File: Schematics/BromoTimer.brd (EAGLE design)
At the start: 49.2 x 71.1 mm, 20 parts, among them IC1 PIC16F687, IC2 7805TV, K1 351, K2 351, Q1 2N3565, Q2 2N3565, X4 22-23-2021

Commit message: Fixed bug in schematics
The poles on the diode bridge were inverted.
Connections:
- net GND: now also B1.-; no longer B1.+
- net V+: now also B1.+; no longer B1.-
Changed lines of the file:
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@@
 <?xml version="1.0" encoding="utf-8"?>
 <!DOCTYPE eagle SYSTEM "eagle.dtd">
-<eagle version="6.2">
+<eagle version="6.3">
 <drawing>
 <settings>
@@
 <contactref element="Q2" pad="3"/>
 <contactref element="C1" pad="-"/>
-<contactref element="B1" pad="+"/>
 <contactref element="SV1" pad="1"/>
 <contactref element="X4" pad="1"/>
-<wire x1="19.05" y1="67.31" x2="46.99" y2="67.31" width="0" layer="19" extent="1-1"/>
-<wire x1="2.54" y1="67.31" x2="19.05" y2="67.31" width="0" layer="19" extent="1-1"/>
-<wire x1="12.7" y1="52.07" x2="19.05" y2="67.31" width="0" layer="19" extent="1-1"/>
-<wire x1="8.382" y1="41.91" x2="12.7" y2="52.07" width="0" layer="19" extent="1-1"/>
-<wire x1="2.54" y1="41.91" x2="8.382" y2="41.91" width="0" layer="19" extent="1-1"/>
-<wire x1="5.08" y1="29.21" x2="2.54" y2="41.91" width="0" layer="19" extent="1-1"/>
-<wire x1="42.545" y1="50.8" x2="2.54" y2="41.91" width="0" layer="19" extent="1-1"/>
+<contactref element="B1" pad="-"/>
+<wire x1="42.545" y1="50.8" x2="46.99" y2="67.31" width="0" layer="19" extent="1-1"/>
 <wire x1="44.45" y1="36.83" x2="42.545" y2="50.8" width="0" layer="19" extent="1-1"/>
 <wire x1="29.21" y1="36.83" x2="44.45" y2="36.83" width="0" layer="19" extent="1-1"/>
-<wire x1="5.08" y1="50.8" x2="29.21" y2="36.83" width="0" layer="19" extent="1-1"/>
+<wire x1="10.16" y1="34.29" x2="29.21" y2="36.83" width="0" layer="19" extent="1-1"/>
+<wire x1="8.382" y1="41.91" x2="10.16" y2="34.29" width="0" layer="19" extent="1-1"/>
+<wire x1="2.54" y1="41.91" x2="8.382" y2="41.91" width="0" layer="19" extent="1-1"/>
+<wire x1="5.08" y1="50.8" x2="2.54" y2="41.91" width="0" layer="19" extent="1-1"/>
+<wire x1="12.7" y1="52.07" x2="5.08" y2="50.8" width="0" layer="19" extent="1-1"/>
 <wire x1="3.81" y1="58.42" x2="5.08" y2="50.8" width="0" layer="19" extent="1-1"/>
+<wire x1="2.54" y1="67.31" x2="3.81" y2="58.42" width="0" layer="19" extent="1-1"/>
+<wire x1="19.05" y1="67.31" x2="12.7" y2="52.07" width="0" layer="19" extent="1-1"/>
 </signal>
 <signal name="RS">
@@
 </signal>
 <signal name="V+">
-<contactref element="B1" pad="-"/>
 <contactref element="C1" pad="+"/>
 <contactref element="IC2" pad="1"/>
-<wire x1="10.16" y1="34.29" x2="11.938" y2="41.91" width="0" layer="19" extent="1-1"/>
-<wire x1="2.54" y1="39.37" x2="10.16" y2="34.29" width="0" layer="19" extent="1-1"/>
+<contactref element="B1" pad="+"/>
+<wire x1="2.54" y1="39.37" x2="11.938" y2="41.91" width="0" layer="19" extent="1-1"/>
+<wire x1="5.08" y1="29.21" x2="2.54" y2="39.37" width="0" layer="19" extent="1-1"/>
 </signal>
 <signal name="N$13">

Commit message: Use 12V relay.
Use 12V relay since V relays are not common.
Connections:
- net +5V: no longer K1.1, K2.1
- net V+: now also K1.1, K2.1
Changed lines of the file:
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@@
 <contactref element="SV2" pad="2"/>
 <contactref element="R1" pad="A"/>
-<contactref element="K1" pad="1"/>
-<contactref element="K2" pad="1"/>
+<wire x1="21.59" y1="67.31" x2="42.545" y2="57.15" width="0" layer="19" extent="1-1"/>
 <wire x1="12.7" y1="59.69" x2="21.59" y2="67.31" width="0" layer="19" extent="1-1"/>
-<wire x1="26.67" y1="31.75" x2="12.7" y2="59.69" width="0" layer="19" extent="1-1"/>
-<wire x1="39.37" y1="31.75" x2="26.67" y2="31.75" width="0" layer="19" extent="1-1"/>
-<wire x1="2.54" y1="44.45" x2="39.37" y2="31.75" width="0" layer="19" extent="1-1"/>
-<wire x1="2.54" y1="50.8" x2="2.54" y2="44.45" width="0" layer="19" extent="1-1"/>
-<wire x1="42.545" y1="57.15" x2="2.54" y2="50.8" width="0" layer="19" extent="1-1"/>
+<wire x1="2.54" y1="50.8" x2="12.7" y2="59.69" width="0" layer="19" extent="1-1"/>
+<wire x1="2.54" y1="44.45" x2="2.54" y2="50.8" width="0" layer="19" extent="1-1"/>
 </signal>
 <signal name="GND">
@@
 <contactref element="IC2" pad="1"/>
 <contactref element="B1" pad="+"/>
+<contactref element="K2" pad="1"/>
+<contactref element="K1" pad="1"/>
+<wire x1="26.67" y1="31.75" x2="39.37" y2="31.75" width="0" layer="19" extent="1-1"/>
+<wire x1="11.938" y1="41.91" x2="26.67" y2="31.75" width="0" layer="19" extent="1-1"/>
 <wire x1="2.54" y1="39.37" x2="11.938" y2="41.91" width="0" layer="19" extent="1-1"/>
 <wire x1="5.08" y1="29.21" x2="2.54" y2="39.37" width="0" layer="19" extent="1-1"/>

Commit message: Add ICSP header
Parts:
- added D1, D2: 1N4148DO35-7, diode:DO35-7
- added SV3: (no value), con-lstb:MA05-1
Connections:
- new net N$15: IC1.4, SV3.1
- net +5V: now also SV3.2
- net A: now also SV3.4
- net B: now also SV3.5
- net GND: now also D1.A, D2.A, SV3.3
- net V+: now also D1.C, D2.C
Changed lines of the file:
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@@
 <attribute name="OC_FARNELL" value="1462926" x="44.45" y="102.87" size="1.778" layer="27" rot="R90" display="off"/>
+</element>
+<element name="D1" library="diode" package="DO35-7" value="1N4148DO35-7" x="3.81" y="-6.35"/>
+<element name="D2" library="diode" package="DO35-7" value="1N4148DO35-7" x="3.81" y="-12.7"/>
+<element name="SV3" library="con-lstb" package="MA05-1" value="" x="5.08" y="-20.32">
+<attribute name="OC_NEWARK" value="unknown" x="5.08" y="-20.32" size="1.778" layer="27" display="off"/>
+<attribute name="MPN" value="" x="5.08" y="-20.32" size="1.778" layer="27" display="off"/>
+<attribute name="MF" value="" x="5.08" y="-20.32" size="1.778" layer="27" display="off"/>
+<attribute name="OC_FARNELL" value="unknown" x="5.08" y="-20.32" size="1.778" layer="27" display="off"/>
 </element>
 </elements>
@@
 <contactref element="SV2" pad="2"/>
 <contactref element="R1" pad="A"/>
+<contactref element="SV3" pad="2"/>
 <wire x1="21.59" y1="67.31" x2="42.545" y2="57.15" width="0" layer="19" extent="1-1"/>
 <wire x1="12.7" y1="59.69" x2="21.59" y2="67.31" width="0" layer="19" extent="1-1"/>
 <wire x1="2.54" y1="50.8" x2="12.7" y2="59.69" width="0" layer="19" extent="1-1"/>
 <wire x1="2.54" y1="44.45" x2="2.54" y2="50.8" width="0" layer="19" extent="1-1"/>
+<wire x1="2.54" y1="-20.32" x2="2.54" y2="44.45" width="0" layer="19" extent="1-1"/>
 </signal>
 <signal name="GND">
@@
 <contactref element="X4" pad="1"/>
 <contactref element="B1" pad="-"/>
+<contactref element="D2" pad="A"/>
+<contactref element="D1" pad="A"/>
+<contactref element="SV3" pad="3"/>
 <wire x1="42.545" y1="50.8" x2="46.99" y2="67.31" width="0" layer="19" extent="1-1"/>
 <wire x1="44.45" y1="36.83" x2="42.545" y2="50.8" width="0" layer="19" extent="1-1"/>
@@
 <wire x1="2.54" y1="67.31" x2="3.81" y2="58.42" width="0" layer="19" extent="1-1"/>
 <wire x1="19.05" y1="67.31" x2="12.7" y2="52.07" width="0" layer="19" extent="1-1"/>
+<wire x1="7.62" y1="-6.35" x2="10.16" y2="34.29" width="0" layer="19" extent="1-1"/>
+<wire x1="7.62" y1="-12.7" x2="7.62" y2="-6.35" width="0" layer="19" extent="1-1"/>
+<wire x1="5.08" y1="-20.32" x2="7.62" y2="-12.7" width="0" layer="19" extent="1-1"/>
 </signal>
 <signal name="RS">
@@
 <contactref element="SV1" pad="5"/>
 <contactref element="IC1" pad="19"/>
+<contactref element="SV3" pad="4"/>
 <wire x1="15.24" y1="59.69" x2="12.7" y2="67.31" width="0" layer="19" extent="1-1"/>
+<wire x1="7.62" y1="-20.32" x2="15.24" y2="59.69" width="0" layer="19" extent="1-1"/>
 </signal>
 <signal name="B">
 <contactref element="SV1" pad="6"/>
 <contactref element="IC1" pad="18"/>
+<contactref element="SV3" pad="5"/>
 <wire x1="17.78" y1="59.69" x2="15.24" y2="67.31" width="0" layer="19" extent="1-1"/>
+<wire x1="10.16" y1="-20.32" x2="17.78" y2="59.69" width="0" layer="19" extent="1-1"/>
 </signal>
 <signal name="N$4">
@@
 <contactref element="K2" pad="1"/>
 <contactref element="K1" pad="1"/>
+<contactref element="D2" pad="C"/>
+<contactref element="D1" pad="C"/>
 <wire x1="26.67" y1="31.75" x2="39.37" y2="31.75" width="0" layer="19" extent="1-1"/>
 <wire x1="11.938" y1="41.91" x2="26.67" y2="31.75" width="0" layer="19" extent="1-1"/>
 <wire x1="2.54" y1="39.37" x2="11.938" y2="41.91" width="0" layer="19" extent="1-1"/>
 <wire x1="5.08" y1="29.21" x2="2.54" y2="39.37" width="0" layer="19" extent="1-1"/>
+<wire x1="0" y1="-6.35" x2="5.08" y2="29.21" width="0" layer="19" extent="1-1"/>
+<wire x1="0" y1="-12.7" x2="0" y2="-6.35" width="0" layer="19" extent="1-1"/>
 </signal>
 <signal name="N$13">
@@
 <wire x1="20.32" y1="41.91" x2="25.4" y2="52.07" width="0" layer="19" extent="1-1"/>
 </signal>
+<signal name="N$15">
+<contactref element="SV3" pad="1"/>
+<contactref element="IC1" pad="4"/>
+<wire x1="0" y1="-20.32" x2="20.32" y2="52.07" width="0" layer="19" extent="1-1"/>
+</signal>
 </signals>

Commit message: Add buzzer and diode protection to 7805.
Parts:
- added D3: 1N4148DO35-7, diode:DO35-7
- added Q3: 2N3565, transistor-npn:TO92
- added R5: (no value), rcl:0207/10
- added X5: 22-23-2021, con-molex:22-23-2021
- SV1: value (none) -> ENCODER
- SV2: value (none) -> DISPLAY
- SV3: value (none) -> ICSP
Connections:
- new net N$17: IC1.5, R5.2
- new net N$18: Q3.2, R5.1
- new net N$19: Q3.3, X5.1
- net +5V: now also D3.A
- net GND: now also Q3.1
- net SW: now also IC1.2
- net V+: now also D3.C, X5.2
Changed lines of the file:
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@@
 <elements>
 <element name="IC1" library="ic-package" package="SOCKET-20" value="PIC16F687" x="24.13" y="55.88"/>
-<element name="SV1" library="con-lsta" package="FE06" value="" x="8.89" y="67.31">
+<element name="SV1" library="con-lsta" package="FE06" value="ENCODER" x="8.89" y="67.31">
 <attribute name="OC_NEWARK" value="unknown" x="62.23" y="7.62" size="1.778" layer="27" display="off"/>
 <attribute name="MPN" value="" x="62.23" y="7.62" size="1.778" layer="27" display="off"/>
@@
 <attribute name="OC_FARNELL" value="unknown" x="62.23" y="7.62" size="1.778" layer="27" display="off"/>
 </element>
-<element name="SV2" library="con-lsta" package="FE12" value="" x="33.02" y="67.31">
+<element name="SV2" library="con-lsta" package="FE12" value="DISPLAY" x="33.02" y="67.31">
 <attribute name="OC_NEWARK" value="unknown" x="62.23" y="7.62" size="1.778" layer="27" display="off"/>
 <attribute name="MPN" value="" x="62.23" y="7.62" size="1.778" layer="27" display="off"/>
@@
 <element name="D1" library="diode" package="DO35-7" value="1N4148DO35-7" x="3.81" y="-6.35"/>
 <element name="D2" library="diode" package="DO35-7" value="1N4148DO35-7" x="3.81" y="-12.7"/>
-<element name="SV3" library="con-lstb" package="MA05-1" value="" x="5.08" y="-20.32">
+<element name="SV3" library="con-lstb" package="MA05-1" value="ICSP" x="5.08" y="-20.32">
 <attribute name="OC_NEWARK" value="unknown" x="5.08" y="-20.32" size="1.778" layer="27" display="off"/>
 <attribute name="MPN" value="" x="5.08" y="-20.32" size="1.778" layer="27" display="off"/>
@@
 <attribute name="OC_FARNELL" value="unknown" x="5.08" y="-20.32" size="1.778" layer="27" display="off"/>
 </element>
+<element name="D3" library="diode" package="DO35-7" value="1N4148DO35-7" x="3.81" y="-27.94"/>
+<element name="Q3" library="transistor-npn" package="TO92" value="2N3565" x="0" y="-34.29"/>
+<element name="R5" library="rcl" package="0207/10" value="" x="3.81" y="-39.37"/>
+<element name="X5" library="con-molex" package="22-23-2021" value="22-23-2021" x="-6.35" y="-34.29">
+<attribute name="OC_NEWARK" value="25C3832" x="-6.35" y="-34.29" size="1.778" layer="27" display="off"/>
+<attribute name="MPN" value="22-23-2021" x="-6.35" y="-34.29" size="1.778" layer="27" display="off"/>
+<attribute name="MF" value="MOLEX" x="-6.35" y="-34.29" size="1.778" layer="27" display="off"/>
+<attribute name="OC_FARNELL" value="1462926" x="-6.35" y="-34.29" size="1.778" layer="27" display="off"/>
+</element>
 </elements>
 <signals>
 <signal name="+5V">
-<contactref element="IC2" pad="3"/>
-<contactref element="C2" pad="+"/>
 <contactref element="IC1" pad="20"/>
 <contactref element="SV2" pad="2"/>
 <contactref element="R1" pad="A"/>
 <contactref element="SV3" pad="2"/>
+<contactref element="IC2" pad="3"/>
+<contactref element="C2" pad="+"/>
+<contactref element="D3" pad="A"/>
 <wire x1="21.59" y1="67.31" x2="42.545" y2="57.15" width="0" layer="19" extent="1-1"/>
 <wire x1="12.7" y1="59.69" x2="21.59" y2="67.31" width="0" layer="19" extent="1-1"/>
@@
 <wire x1="2.54" y1="44.45" x2="2.54" y2="50.8" width="0" layer="19" extent="1-1"/>
 <wire x1="2.54" y1="-20.32" x2="2.54" y2="44.45" width="0" layer="19" extent="1-1"/>
+<wire x1="7.62" y1="-27.94" x2="2.54" y2="-20.32" width="0" layer="19" extent="1-1"/>
 </signal>
 <signal name="GND">
@@
 <contactref element="D1" pad="A"/>
 <contactref element="SV3" pad="3"/>
+<contactref element="Q3" pad="1"/>
 <wire x1="42.545" y1="50.8" x2="46.99" y2="67.31" width="0" layer="19" extent="1-1"/>
 <wire x1="44.45" y1="36.83" x2="42.545" y2="50.8" width="0" layer="19" extent="1-1"/>
@@
 <wire x1="7.62" y1="-12.7" x2="7.62" y2="-6.35" width="0" layer="19" extent="1-1"/>
 <wire x1="5.08" y1="-20.32" x2="7.62" y2="-12.7" width="0" layer="19" extent="1-1"/>
+<wire x1="1.27" y1="-34.29" x2="5.08" y2="-20.32" width="0" layer="19" extent="1-1"/>
 </signal>
 <signal name="RS">
@@
 <signal name="SW">
 <contactref element="SV1" pad="4"/>
+<contactref element="IC1" pad="2"/>
+<wire x1="15.24" y1="52.07" x2="10.16" y2="67.31" width="0" layer="19" extent="1-1"/>
 </signal>
 <signal name="A">
@@
 <contactref element="D2" pad="C"/>
 <contactref element="D1" pad="C"/>
+<contactref element="D3" pad="C"/>
+<contactref element="X5" pad="2"/>
 <wire x1="26.67" y1="31.75" x2="39.37" y2="31.75" width="0" layer="19" extent="1-1"/>
 <wire x1="11.938" y1="41.91" x2="26.67" y2="31.75" width="0" layer="19" extent="1-1"/>
@@
 <wire x1="0" y1="-6.35" x2="5.08" y2="29.21" width="0" layer="19" extent="1-1"/>
 <wire x1="0" y1="-12.7" x2="0" y2="-6.35" width="0" layer="19" extent="1-1"/>
+<wire x1="0" y1="-27.94" x2="0" y2="-12.7" width="0" layer="19" extent="1-1"/>
+<wire x1="-5.08" y1="-34.29" x2="0" y2="-27.94" width="0" layer="19" extent="1-1"/>
 </signal>
 <signal name="N$13">
@@
 <wire x1="0" y1="-20.32" x2="20.32" y2="52.07" width="0" layer="19" extent="1-1"/>
 </signal>
+<signal name="N$17">
+<contactref element="R5" pad="2"/>
+<contactref element="IC1" pad="5"/>
+<wire x1="8.89" y1="-39.37" x2="22.86" y2="52.07" width="0" layer="19" extent="1-1"/>
+</signal>
+<signal name="N$18">
+<contactref element="R5" pad="1"/>
+<contactref element="Q3" pad="2"/>
+<wire x1="0" y1="-32.385" x2="-1.27" y2="-39.37" width="0" layer="19" extent="1-1"/>
+</signal>
+<signal name="N$19">
+<contactref element="Q3" pad="3"/>
+<contactref element="X5" pad="1"/>
+<wire x1="-1.27" y1="-34.29" x2="-7.62" y2="-34.29" width="0" layer="19" extent="1-1"/>
+</signal>
 </signals>

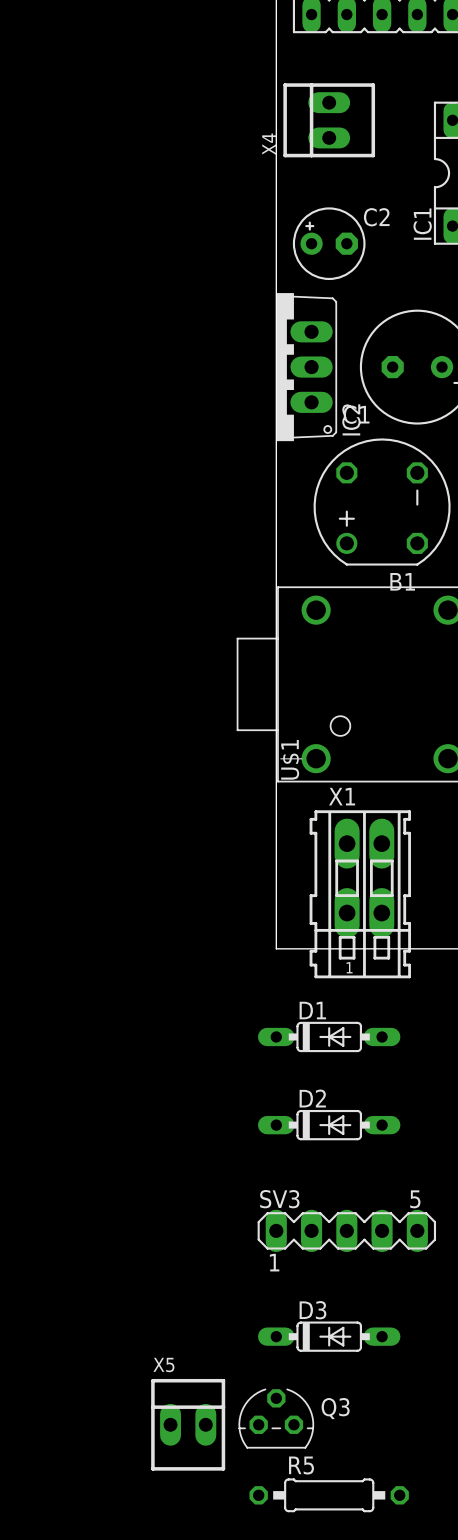
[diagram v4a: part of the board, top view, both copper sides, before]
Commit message: Add support for external LED
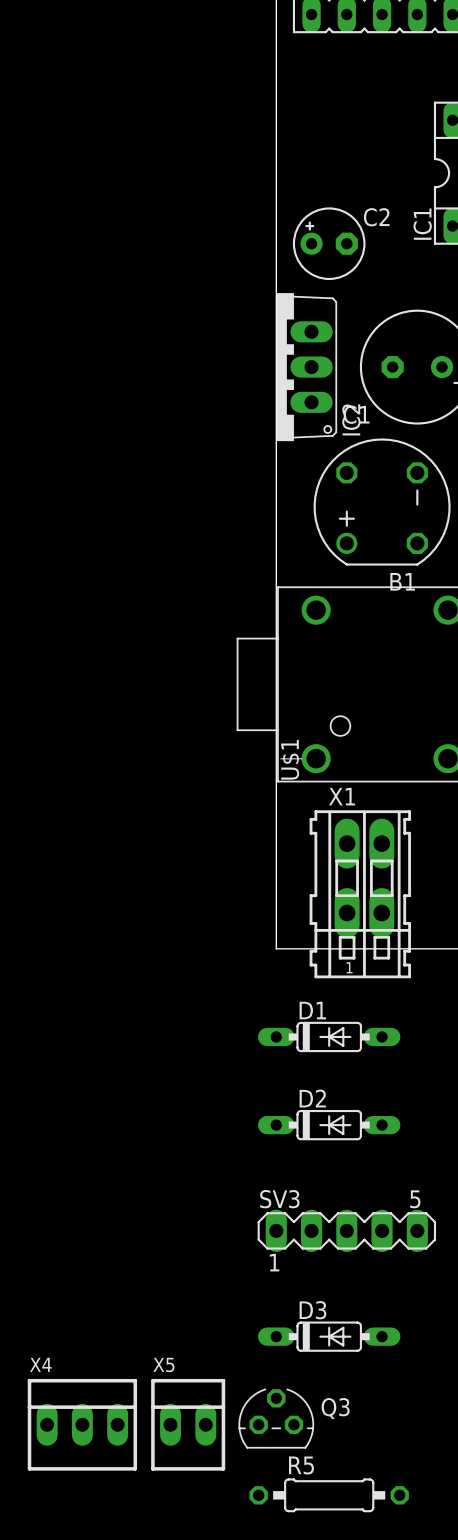
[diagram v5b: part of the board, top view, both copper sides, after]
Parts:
- X4: value 22-23-2021 -> 22-23-2031; device con-molex:22-23-2021 -> con-molex:22-23-2031
- X5: value 22-23-2021 -> BUZZER
- moved X4 95.6 mm to (-14.0, -34.3), turned to 0 degrees
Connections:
- new net N$20: IC1.3, X4.1
- net GND: now also X4.3; no longer X4.1
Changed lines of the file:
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@@
 <element name="U$1" library="SparkFun" package="TRANSFORMER" value="TRANSFORMERPTH" x="7.62" y="19.05" rot="R90"/>
 <element name="B1" library="rectifier" package="RB1A" value="" x="7.62" y="31.75" rot="R90"/>
-<element name="X4" library="con-molex" package="22-23-2021" value="22-23-2021" x="3.81" y="59.69" rot="R90">
-<attribute name="OC_NEWARK" value="25C3832" x="44.45" y="102.87" size="1.778" layer="27" rot="R90" display="off"/>
-<attribute name="MPN" value="22-23-2021" x="44.45" y="102.87" size="1.778" layer="27" rot="R90" display="off"/>
-<attribute name="MF" value="MOLEX" x="44.45" y="102.87" size="1.778" layer="27" rot="R90" display="off"/>
-<attribute name="OC_FARNELL" value="1462926" x="44.45" y="102.87" size="1.778" layer="27" rot="R90" display="off"/>
-</element>
 <element name="D1" library="diode" package="DO35-7" value="1N4148DO35-7" x="3.81" y="-6.35"/>
 <element name="D2" library="diode" package="DO35-7" value="1N4148DO35-7" x="3.81" y="-12.7"/>
@@
 <element name="Q3" library="transistor-npn" package="TO92" value="2N3565" x="0" y="-34.29"/>
 <element name="R5" library="rcl" package="0207/10" value="" x="3.81" y="-39.37"/>
-<element name="X5" library="con-molex" package="22-23-2021" value="22-23-2021" x="-6.35" y="-34.29">
+<element name="X5" library="con-molex" package="22-23-2021" value="BUZZER" x="-6.35" y="-34.29">
 <attribute name="OC_NEWARK" value="25C3832" x="-6.35" y="-34.29" size="1.778" layer="27" display="off"/>
 <attribute name="MPN" value="22-23-2021" x="-6.35" y="-34.29" size="1.778" layer="27" display="off"/>
 <attribute name="MF" value="MOLEX" x="-6.35" y="-34.29" size="1.778" layer="27" display="off"/>
 <attribute name="OC_FARNELL" value="1462926" x="-6.35" y="-34.29" size="1.778" layer="27" display="off"/>
+</element>
+<element name="X4" library="con-molex" package="22-23-2031" value="22-23-2031" x="-13.97" y="-34.29">
+<attribute name="OC_NEWARK" value="30C0862" x="-13.97" y="-34.29" size="1.778" layer="27" display="off"/>
+<attribute name="MPN" value="22-23-2031" x="-13.97" y="-34.29" size="1.778" layer="27" display="off"/>
+<attribute name="MF" value="MOLEX" x="-13.97" y="-34.29" size="1.778" layer="27" display="off"/>
+<attribute name="OC_FARNELL" value="1462950" x="-13.97" y="-34.29" size="1.778" layer="27" display="off"/>
 </element>
 </elements>
@@
 <contactref element="C1" pad="-"/>
 <contactref element="SV1" pad="1"/>
-<contactref element="X4" pad="1"/>
 <contactref element="B1" pad="-"/>
 <contactref element="D2" pad="A"/>
@@
 <contactref element="SV3" pad="3"/>
 <contactref element="Q3" pad="1"/>
+<contactref element="X4" pad="3"/>
 <wire x1="42.545" y1="50.8" x2="46.99" y2="67.31" width="0" layer="19" extent="1-1"/>
 <wire x1="44.45" y1="36.83" x2="42.545" y2="50.8" width="0" layer="19" extent="1-1"/>
@@
 <wire x1="5.08" y1="50.8" x2="2.54" y2="41.91" width="0" layer="19" extent="1-1"/>
 <wire x1="12.7" y1="52.07" x2="5.08" y2="50.8" width="0" layer="19" extent="1-1"/>
-<wire x1="3.81" y1="58.42" x2="5.08" y2="50.8" width="0" layer="19" extent="1-1"/>
-<wire x1="2.54" y1="67.31" x2="3.81" y2="58.42" width="0" layer="19" extent="1-1"/>
 <wire x1="19.05" y1="67.31" x2="12.7" y2="52.07" width="0" layer="19" extent="1-1"/>
+<wire x1="2.54" y1="67.31" x2="19.05" y2="67.31" width="0" layer="19" extent="1-1"/>
 <wire x1="7.62" y1="-6.35" x2="10.16" y2="34.29" width="0" layer="19" extent="1-1"/>
 <wire x1="7.62" y1="-12.7" x2="7.62" y2="-6.35" width="0" layer="19" extent="1-1"/>
 <wire x1="5.08" y1="-20.32" x2="7.62" y2="-12.7" width="0" layer="19" extent="1-1"/>
 <wire x1="1.27" y1="-34.29" x2="5.08" y2="-20.32" width="0" layer="19" extent="1-1"/>
+<wire x1="-11.43" y1="-34.29" x2="1.27" y2="-34.29" width="0" layer="19" extent="1-1"/>
 </signal>
 <signal name="RS">
@@
 <wire x1="-5.08" y1="-34.29" x2="0" y2="-27.94" width="0" layer="19" extent="1-1"/>
 </signal>
-<signal name="N$13">
-<contactref element="X4" pad="2"/>
-<contactref element="IC1" pad="17"/>
-<wire x1="3.81" y1="60.96" x2="20.32" y2="59.69" width="0" layer="19" extent="1-1"/>
-</signal>
 <signal name="N$16">
 <contactref element="R3" pad="1"/>
@@
 <wire x1="-1.27" y1="-34.29" x2="-7.62" y2="-34.29" width="0" layer="19" extent="1-1"/>
 </signal>
+<signal name="N$13">
+<contactref element="IC1" pad="17"/>
+<contactref element="X4" pad="2"/>
+<wire x1="-13.97" y1="-34.29" x2="20.32" y2="59.69" width="0" layer="19" extent="1-1"/>
+</signal>
+<signal name="N$20">
+<contactref element="X4" pad="1"/>
+<contactref element="IC1" pad="3"/>
+<wire x1="-16.51" y1="-34.29" x2="17.78" y2="52.07" width="0" layer="19" extent="1-1"/>
+</signal>
 </signals>
